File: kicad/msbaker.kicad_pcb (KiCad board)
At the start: 4 copper layers, 14 x 62 mm, 48 parts, among them J1 USB_B_Micro, J2 Micro_SD_Card, J3 GPIO, M2 MountingHole_2.2mm_M2_ISO1458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, U1 MIC5365-3.3YC5, U2 W25Q128JVS, U3 RP2040, U4 LSM6DSO32, Y1 12MHz

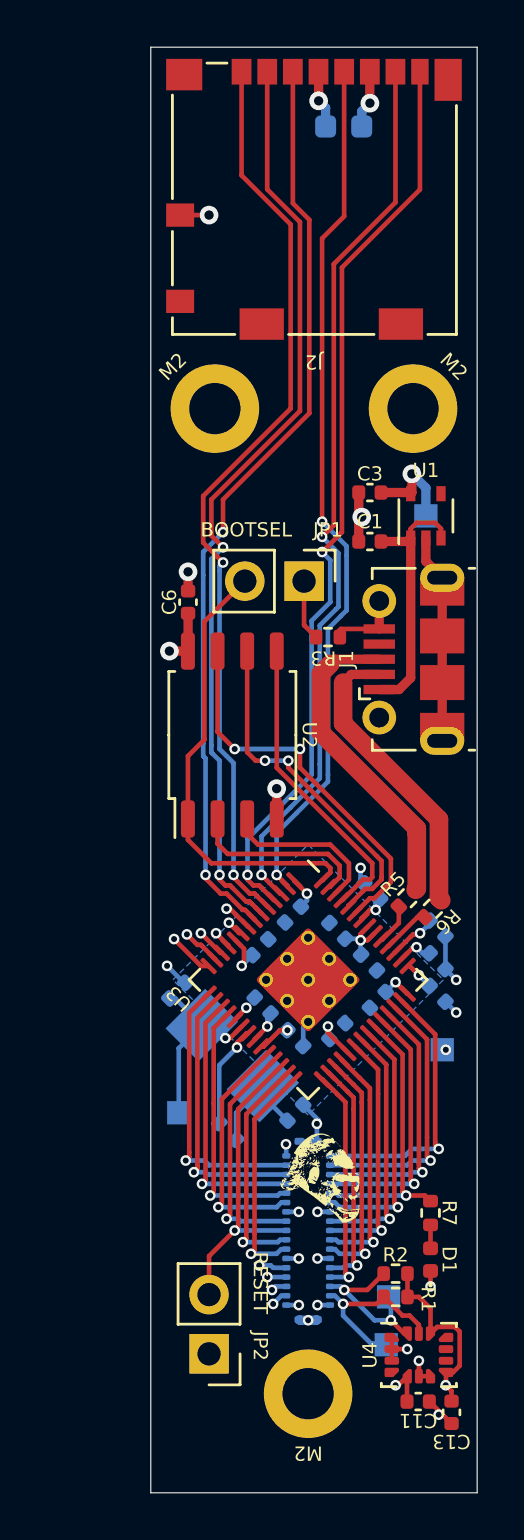
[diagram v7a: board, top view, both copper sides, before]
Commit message: Changed IMU to SPI and shrunk board
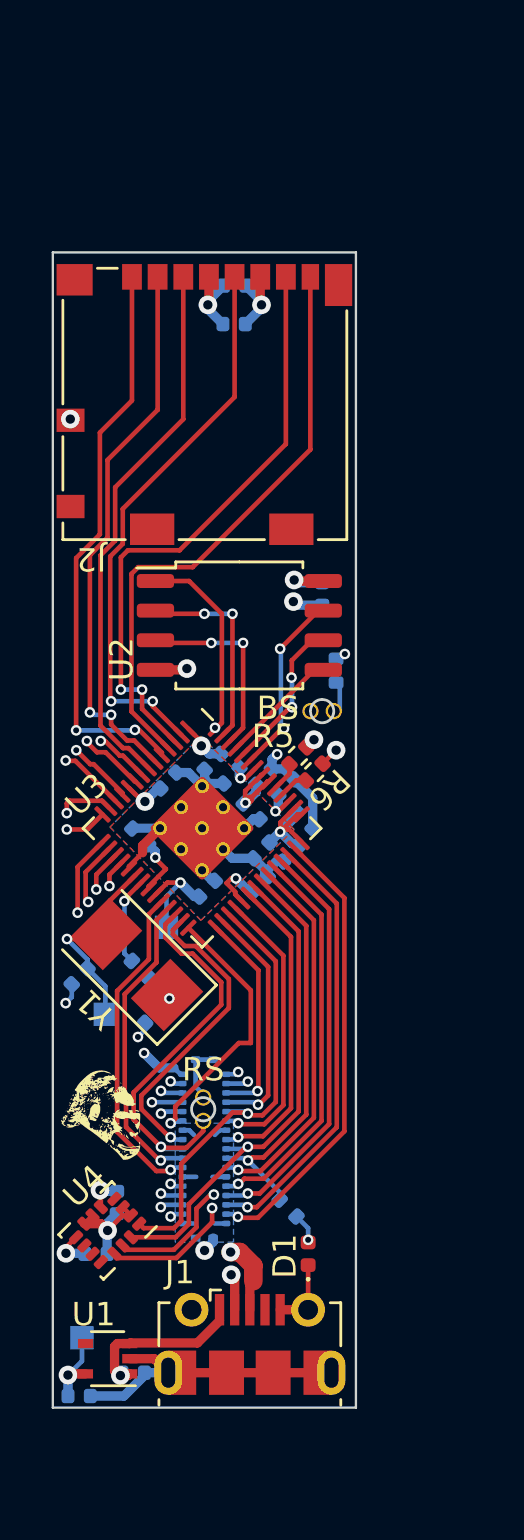
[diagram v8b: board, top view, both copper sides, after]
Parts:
- removed JP1: BOOTSEL, Connector_PinHeader_2.54mm:PinHeader_1x02_P2.54mm_Vertical
- removed JP2: RESET, Connector_PinHeader_2.54mm:PinHeader_1x02_P2.54mm_Vertical
- removed M2 (x3): MountingHole_2.2mm_M2_ISO14580_Pad, MountingHole:MountingHole_2.2mm_M2_ISO14580_Pad
- removed R1, R2: 15k, Resistor_SMD:R_0402_1005Metric
- removed TP4: I2C SDA, TestPoint:TestPoint_Pad_1.0x1.0mm
- removed TP5: I2C SCL, TestPoint:TestPoint_Pad_1.0x1.0mm
- added BS: BOOTSEL, msbaker:poke_jumper, F.Cu at (148.8, 102.5)
- added C21: 4.7u, Capacitor_SMD:C_0402_1005Metric, B.Cu at (145.1, 85.9)
- added RS: RESET, msbaker:poke_jumper, F.Cu at (143.8, 119.5)
- C1, C11, C13, C3, C6, R3: moved to B.Cu
- C2: value 10u -> 4.7u; footprint Capacitor_SMD:C_0603_1608Metric -> Capacitor_SMD:C_0402_1005Metric
- R7: value 480 -> 470; moved to B.Cu
- Y1: moved to F.Cu
- moved C3 40.7 mm to (138.4, 131.8), turned to 0 degrees
- moved U1 38.6 mm to (139.7, 130.2), turned to 180 degrees
- moved TP2 38.2 mm to (138.6, 129.3)
- moved C1 37.1 mm to (140.8, 130.8), turned to 0 degrees
- moved J1 30.2 mm to (145.8, 129.6), turned to 0 degrees
- moved C13 16.7 mm to (139.2, 125.8), turned to 0 degrees
- moved C11 15.5 mm to (140.1, 123.5), turned to -90 degrees
- moved U4 14.4 mm to (139.7, 124.8), turned to -135 degrees
- moved TP1 12.9 mm to (142.2, 111.8)
- moved G*** 9.98 mm to (143.8, 92.0)
- moved J2 9.98 mm to (143.8, 89.3)
- moved G*** 9.78 mm to (139.3, 119.8)
- moved C10 9.74 mm to (146.2, 108.5), turned to -135 degrees
- moved C12 9.15 mm to (146.4, 105.3), turned to 45 degrees
- moved C16 8.95 mm to (141.1, 107.8)
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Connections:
- J3 pad 1: /GPIO29 -> /GPIO7
- J3 pad 10: /GPIO15 -> /GPIO11
- J3 pad 11: /GPIO24 -> /SPI0_CS
- J3 pad 12: /SWCLK -> /GPIO17
- J3 pad 15: /GPIO23 -> /SPI0_SCK
- J3 pad 16: /SWD -> /GPIO16
- J3 pad 17: /GPIO22 -> /SPI0_TX
- J3 pad 19: /GPIO21 -> /LED/UART1_TX
- J3 pad 20: /GPIO16 -> /SWD
- J3 pad 21: /GPIO20 -> /UART1_RX
- J3 pad 22: /GPIO17 -> /SWCLK
- J3 pad 25: /GPIO19 -> /GPIO26
- J3 pad 26: /GPIO11 -> /GPIO15
- J3 pad 27: /GPIO18 -> /GPIO27
- J3 pad 28: /GPIO10 -> /GPIO14
- J3 pad 29: /I2C0_SDA -> /GPIO28
- J3 pad 3: /GPIO28 -> /GPIO6
- J3 pad 30: /GPIO9 -> /GPIO13
- J3 pad 31: /I2C0_SCL -> /GPIO29
- J3 pad 32: /GPIO8 -> /GPIO12
- J3 pad 4: /GPIO12 -> /GPIO8
- J3 pad 5: /GPIO27 -> /GPIO18
- J3 pad 6: /GPIO13 -> /GPIO9
- J3 pad 7: /GPIO26 -> /GPIO19
- J3 pad 8: /GPIO14 -> /GPIO10
- J3 pad 9: /LED -> /SPI0_RX
- R7 pad 1: /LED -> /LED/UART1_TX
- U3 pad 31: /GPIO20 -> /SPI0_RX
- U3 pad 32: /GPIO21 -> /SPI0_CS
- U3 pad 34: /GPIO22 -> /SPI0_SCK
- U3 pad 35: /GPIO23 -> /SPI0_TX
- U3 pad 36: /GPIO24 -> /LED/UART1_TX
- U3 pad 37: /LED -> /UART1_RX
- U3 pad 8: /I2C0_SDA -> /GPIO6
- U3 pad 9: /I2C0_SCL -> /GPIO7
- U4 pad 1: GND -> /SPI0_RX
- U4 pad 12: +3.3V -> /SPI0_CS
- U4 pad 13: /I2C0_SCL -> /SPI0_SCK
- U4 pad 14: /I2C0_SDA -> /SPI0_TX
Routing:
- net /I2C0_SCL: track 27.4 -> 0.00 mm, vias 2 -> 0
- net /I2C0_SDA: track 27.3 -> 0.00 mm, vias 3 -> 0
- net /SPI0_CS: track 0.00 -> 22.1 mm, vias 0 -> 2
- net /SPI0_SCK: track 0.00 -> 21.6 mm, vias 0 -> 2
- net /SPI0_TX: track 0.00 -> 21.2 mm, vias 0 -> 1
- net /GPIO6: track 0.00 -> 20.6 mm, vias 0 -> 2
- net /GPIO7: track 0.00 -> 20.3 mm, vias 0 -> 2
- net /SPI0_RX: track 0.00 -> 19.5 mm, vias 0 -> 1
- net GND: track 37.4 -> 55.9 mm, vias 22 -> 10
- net /LED/UART1_TX: track 0.00 -> 17.3 mm, vias 0 -> 1
- net /SD_CMD: track 39.7 -> 23.5 mm, vias 2 -> 0
- net /UART1_RX: track 0.00 -> 16.0 mm, vias 0 -> 1
- net /SD_DAT3: track 39.8 -> 23.8 mm
- net /SD_DAT2: track 39.6 -> 24.7 mm
- net /USB_D-: track 12.8 -> 26.9 mm, vias 0 -> 2
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- added copper zone on F.Cu, net +3.3V
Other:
- board size 14 x 62 mm -> 13 x 49.5 mm
